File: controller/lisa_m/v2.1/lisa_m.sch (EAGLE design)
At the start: 119 parts, among them IC9 LP2992 5V, J1 CONN_3-1, J2 CONN_3-1, J3 CONN_3-1, J4 CONN_3-1, J5 CONN_3-1, J6 CONN_3-1, J7 CONN_3-1, J8 CONN_3-1, Q1 12Mhz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

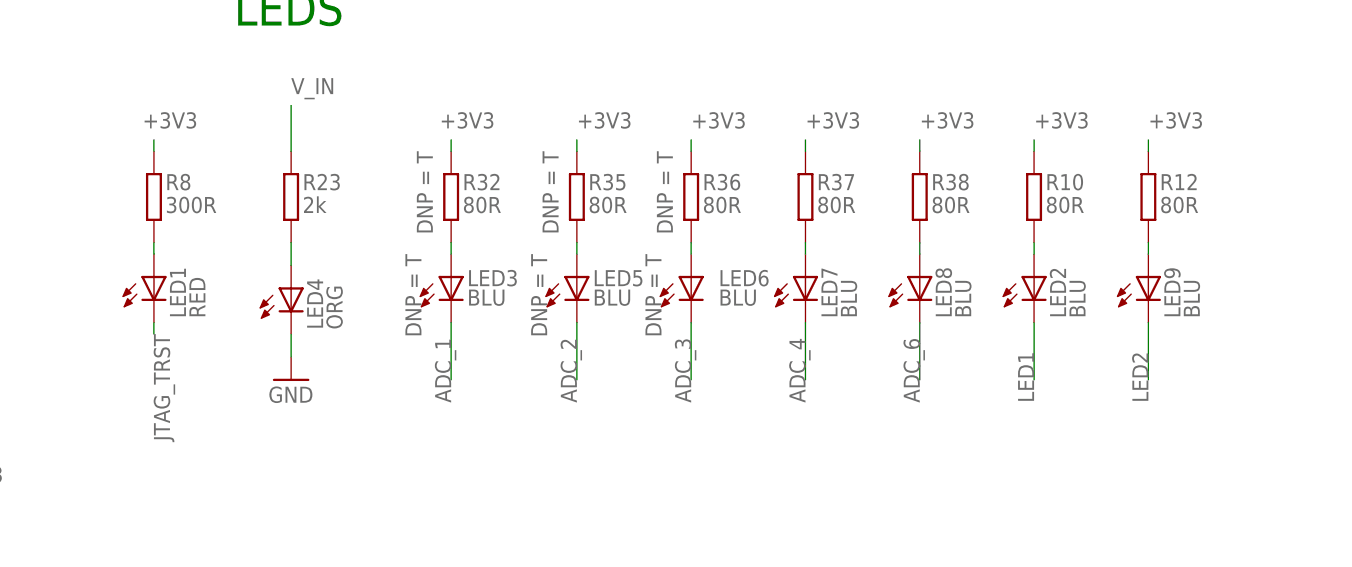
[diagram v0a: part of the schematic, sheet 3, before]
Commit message: changed LED labeling to be more intuitive for a user, both on schematic and on silkscreens, also changed power led schematic name to LEDVIN to keep better consistency with silkscreen and remove number since it can't be controlled
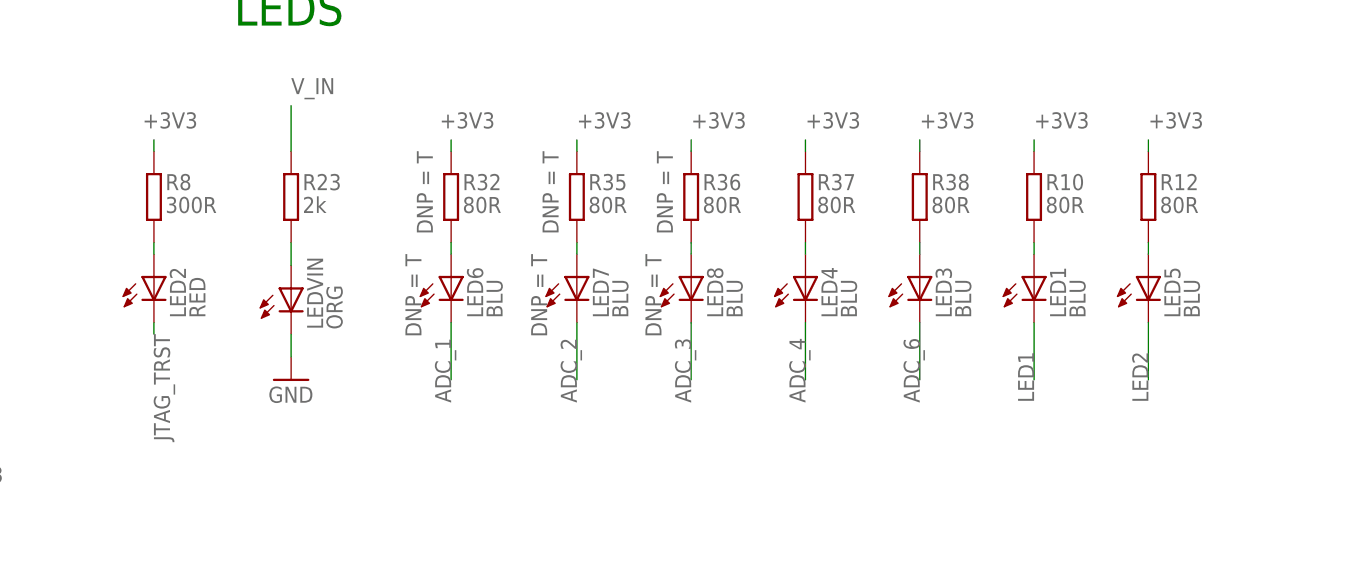
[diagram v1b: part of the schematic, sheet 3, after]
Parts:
- removed LED9: BLU, pel_dipol_comp:LED-0402
- added LEDVIN: ORG, pel_dipol_comp:LED-0402
- LED1: value RED -> BLU; PARTNO SML-P11UTT86 -> SMLP12BC7TT86
- LED2: value BLU -> RED; PARTNO SMLP12BC7TT86 -> SML-P11UTT86
- LED3, LED5: DNP T -> (none)
- LED4: value ORG -> BLU; PARTNO SML-P11DTT86 -> SMLP12BC7TT86
- LED7, LED8: DNP (none) -> T
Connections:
- net ADC_1: now also LED6.C; no longer LED3.C
- net ADC_2: now also LED7.C; no longer LED5.C
- net ADC_3: now also LED8.C; no longer LED6.C
- net ADC_4: now also LED4.C; no longer LED7.C
- net ADC_6: now also LED3.C; no longer LED8.C
- net GND: now also LEDVIN.C; no longer LED4.C
- net JTAG_TRST: now also LED2.C; no longer LED1.C
- net LED1: now also LED1.C; no longer LED2.C
- net LED2: now also LED5.C; no longer LED9.C
- net N$10: now also LED2.A; no longer LED1.A
- net N$11: now also LED8.A; no longer LED6.A
- net N$12: now also LEDVIN.A; no longer LED4.A
- net N$13: now also LED5.A; no longer LED9.A
- net N$14: now also LED4.A; no longer LED7.A
- net N$15: now also LED3.A; no longer LED8.A
- net N$4: now also LED1.A; no longer LED2.A
- net N$5: now also LED6.A; no longer LED3.A
- net N$9: now also LED7.A; no longer LED5.A
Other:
- moved on the sheet: LED1, LED2, LED3, LED4, LED5, LED6, LED7, LED8
